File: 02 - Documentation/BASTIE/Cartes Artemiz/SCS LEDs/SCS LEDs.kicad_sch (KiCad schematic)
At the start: 16 parts, among them J1 2P Droit 2-11-2022, J2 2P Droit 2-11-2022, K1 SSR CPC1394GR, U1 ${SIM.PARAMS}, U2 Opamp_Dual, U3 Alim LP TSR_0.5-2450

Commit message: Encore qlq corrections
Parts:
- removed C2: C, Capacitor_THT:CP_Radial_D5.0mm_P2.00mm, symbol Device:C
- added C2: 10n, EPSA_lib:CAPC2012X130N, symbol EPSA_lib:Condensateur 0805Y1000104JXT
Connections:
- net +5V: now also C2.2
- net GND: now also C2.1
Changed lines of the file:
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@@
     (stroke (width 0) (type default))
   )
-  (polyline (pts (xy 173.99 151.13) (xy 226.06 151.13))
+  (polyline (pts (xy 173.99 152.4) (xy 226.06 152.4))
     (stroke (width 0) (type default))
   )
@@
     (stroke (width 0) (type default))
   )
-  (polyline (pts (xy 173.99 109.22) (xy 173.99 151.13))
+  (polyline (pts (xy 173.99 109.22) (xy 173.99 152.4))
     (stroke (width 0) (type default))
   )
@@
     (stroke (width 0) (type default))
   )
-  (polyline (pts (xy 226.06 151.13) (xy 226.06 109.22))
+  (polyline (pts (xy 226.06 152.4) (xy 226.06 109.22))
     (stroke (width 0) (type default))
   )
@@
     )
   )
+  (symbol (lib_id "EPSA_lib:Condensateur 0805Y1000104JXT") (at 217.17 148.59 90) (unit 1)
+    (in_bom yes) (on_board yes) (dnp no) (fields_autoplaced)
+    (property "Reference" "C2" (at 220.98 139.7 90)
+      (effects (font (size 1.27 1.27)) (justify right))
+    )
+    (property "Value" "10n" (at 220.98 142.24 90)
+      (effects (font (size 1.27 1.27)) (justify right))
+    )
+    (property "Footprint" "EPSA_lib:CAPC2012X130N" (at 217.17 128.27 0)
+      (effects (font (size 1.27 1.27)) (justify left) hide)
+    )
+    (property "Datasheet" "http://docs-europe.electrocomponents.com/webdocs/119d/0900766b8119d7bc.pdf" (at 219.71 128.27 0)
+      (effects (font (size 1.27 1.27)) (justify left) hide)
+    )
+    (property "Sim.Pins" "1=+ 2=-" (at 214.884 123.444 0)
+      (effects (font (size 1.27 1.27)) hide)
+    )
+    (property "Sim.Device" "C" (at 212.09 128.27 0)
+      (effects (font (size 1.27 1.27)) (justify left) hide)
+    )
+    (property "Description" "Syfer 0805 Ceramic Chip Capacitors" (at 222.25 128.27 0)
+      (effects (font (size 1.27 1.27)) (justify left) hide)
+    )
+    (property "Height" "1.3" (at 224.79 128.27 0)
+      (effects (font (size 1.27 1.27)) (justify left) hide)
+    )
+    (property "Manufacturer_Name" "Syfer" (at 227.33 128.27 0)
+      (effects (font (size 1.27 1.27)) (justify left) hide)
+    )
+    (property "Manufacturer_Part_Number" "0805Y1000104JXT" (at 229.87 128.27 0)
+      (effects (font (size 1.27 1.27)) (justify left) hide)
+    )
+    (property "Mouser Part Number" "" (at 231.14 139.7 0)
+      (effects (font (size 1.27 1.27)) (justify left) hide)
+    )
+    (property "Mouser Price/Stock" "" (at 229.87 128.27 0)
+      (effects (font (size 1.27 1.27)) (justify left) hide)
+    )
+    (property "Render Name" "Condensateur" (at 220.98 144.78 90)
+      (effects (font (size 1.27 1.27)) (justify right))
+    )
+    (pin "1")
+    (pin "2")
+    (instances
+      (project "SCS LEDs"
+        (path "/517051b6-4db9-459f-9eb8-ac2447aa7de0"
+          (reference "C2") (unit 1)
+        )
+      )
+    )
+  )
   (symbol (lib_id "power:+12V") (at 172.72 83.82 90) (unit 1)
     (in_bom yes) (on_board yes) (dnp no) (fields_autoplaced)
@@
     )
   )
-  (symbol (lib_id "power:GND") (at 217.17 143.51 0) (unit 1)
-    (in_bom yes) (on_board yes) (dnp no) (fields_autoplaced)
-    (property "Reference" "#GND06" (at 217.17 146.05 0)
-      (effects (font (size 1.27 1.27)) hide)
-    )
-    (property "Value" "0" (at 217.17 140.97 0)
-      (effects (font (size 1.27 1.27)))
-    )
-    (property "Footprint" "" (at 217.17 143.51 0)
-      (effects (font (size 1.27 1.27)) hide)
-    )
-    (property "Datasheet" "~" (at 217.17 143.51 0)
+  (symbol (lib_id "power:GND") (at 217.17 148.59 0) (unit 1)
+    (in_bom yes) (on_board yes) (dnp no) (fields_autoplaced)
+    (property "Reference" "#GND06" (at 217.17 151.13 0)
+      (effects (font (size 1.27 1.27)) hide)
+    )
+    (property "Value" "0" (at 217.17 146.05 0)
+      (effects (font (size 1.27 1.27)))
+    )
+    (property "Footprint" "" (at 217.17 148.59 0)
+      (effects (font (size 1.27 1.27)) hide)
+    )
+    (property "Datasheet" "~" (at 217.17 148.59 0)
       (effects (font (size 1.27 1.27)) hide)
     )
@@
         )
       )
-    )
-  )
-  (symbol (lib_id "Device:C") (at 217.17 139.7 180) (unit 1)
-    (in_bom yes) (on_board yes) (dnp no)
-    (property "Reference" "C2" (at 215.9 135.89 90)
-      (effects (font (size 1.27 1.27)))
-    )
-    (property "Value" "C" (at 215.9 142.24 90)
-      (effects (font (size 1.27 1.27)))
-    )
-    (property "Footprint" "Capacitor_THT:CP_Radial_D5.0mm_P2.00mm" (at 216.2048 135.89 0)
-      (effects (font (size 1.27 1.27)) hide)
-    )
-    (property "Datasheet" "~" (at 217.17 139.7 0)
-      (effects (font (size 1.27 1.27)) hide)
-    )
-    (pin "1")
-    (pin "2")
-    (instances
-      (project "SCS LEDs"
-        (path "/517051b6-4db9-459f-9eb8-ac2447aa7de0"
-          (reference "C2") (unit 1)
-        )
-      )
-      (project "AMS_IMD_Reset"
-        (path "/7d9bad3e-6cf2-4a61-8644-78bfbb2e310d"
-          (reference "C3") (unit 1)
-        )
-      )
-      (project "Discharge Controller"
-        (path "/aef688cc-a50d-4496-8d50-e7a8695060e9"
-          (reference "C2") (unit 1)
-        )
-      )

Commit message: Corrections mineures
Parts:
- added C3, C4: 10n, EPSA_lib:CAPC2012X130N, symbol EPSA_lib:Condensateur 0805Y1000104JXT
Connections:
- net +5V: now also C3.2, C4.2
- net GND: now also C3.1, C4.1

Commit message: Kicadlib + Modifs cartes
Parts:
- added R8: 10k, EPSA_lib:RESC3216X70N, symbol EPSA_lib:Résistance RK73H2BLTDD2152F
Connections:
- net +5V: now also R8.1
- net LED_On: now also R8.2
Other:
- moved on the sheet: U1, U2C

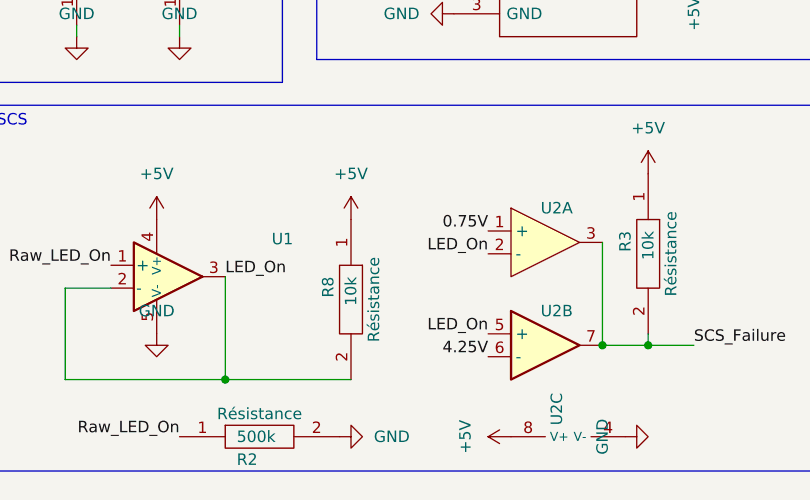
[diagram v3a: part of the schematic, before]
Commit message: Modifications cartes
Prise en compte des retours ECT + PCBs
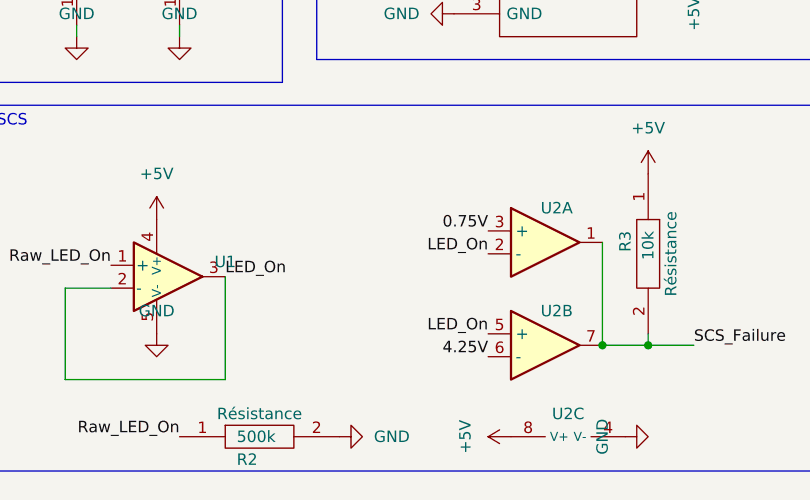
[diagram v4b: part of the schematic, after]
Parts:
- removed R8: 10k, EPSA_lib:RESC3216X70N, symbol EPSA_lib:Résistance RK73H2BLTDD2152F
- U2: symbol EPSA_lib:Opamp_Dual -> EPSA_lib:Comparator_Dual; Manufacturer_Part_Number TLV9062QPWRQ1 -> LMV393IPWR; Mouser Part Number 595-TLV9062QPWRQ1 -> 595-LMV393IPWR
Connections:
- net 0.75V: now also U2.3 (+); no longer U2.1 (+)
- net SCS_Failure: now also U2.1; no longer U2.3
